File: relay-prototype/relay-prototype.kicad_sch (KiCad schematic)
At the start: 13 parts, among them K1 G5V-1

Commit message: schematic for adder, subtractor
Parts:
- removed K1, K? (x4): G5V-1, Relay_THT:Relay_SPDT_Omron_G5V-1, symbol Relay:G5V-1
- A0, A1, B0, B1: footprint (none) -> Button_Switch_THT:SW_DIP_SPSTx01_Slide_9.78x4.72mm_W7.62mm_P2.54mm
- R1, R2, R3, R4: footprint (none) -> Resistor_THT:R_Axial_DIN0207_L6.3mm_D2.5mm_P10.16mm_Horizontal
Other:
- added sheet page1 (page1.kicad_sch)

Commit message: prototype schematic finished for now
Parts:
- added D1 (x5): D_TVS, Diode_THT:D_DO-15_P12.70mm_Horizontal, symbol Device:D_TVS
- added K1 (x5): G5V-1, Relay_THT:Relay_SPDT_Omron_G5V-1, symbol Relay:G5V-1
- added LED1, LED2, LED3, LED4: LED, symbol Device:LED
- added R5, R6, R7, R8: 300, Resistor_THT:R_Axial_DIN0207_L6.3mm_D2.5mm_P10.16mm_Horizontal, symbol Device:R
- added R9: 100k, Resistor_THT:R_Axial_DIN0207_L6.3mm_D2.5mm_P10.16mm_Horizontal, symbol Device:R
- added S1: SW_DIP_x01, Button_Switch_THT:SW_DIP_SPSTx01_Slide_9.78x4.72mm_W7.62mm_P2.54mm, symbol Switch:SW_DIP_x01
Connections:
- net +5V: now also K1.10, K1.10, K1.10, K1.10, K1.10, S1.1
- net A0: now also K1.5, K1.6; no longer A0.2, R1.2
- net A1: now also K1.5, K1.6; no longer A1.2, R2.2
- net B0: now also K1.5, K1.6; no longer B0.2, R3.2
- net B1: now also K1.5, K1.6; no longer B1.2, R4.2
- net GND: now also D1.1 (A1), D1.1 (A1), D1.1 (A1), D1.1 (A1), D1.1 (A1), K1.1, K1.1, K1.1, K1.1, K1.1, K1.2, K1.2, K1.2, K1.2, K1.2, LED1.1 (K), LED2.1 (K), LED3.1 (K), LED4.1 (K), R9.2
- new net: D1.2 (A2), K1.9, R9.1, S1.2
- new net: A1.2, D1.2 (A2), K1.9, R2.2, R6.1
- new net: B1.2, D1.2 (A2), K1.9, R4.2, R8.1
- new net: A0.2, D1.2 (A2), K1.9, R1.2, R5.1
- new net: LED1.2 (A), R5.2
- new net: LED4.2 (A), R8.2
- new net: LED3.2 (A), R7.2
- new net: B0.2, D1.2 (A2), K1.9, R3.2, R7.1
- new net: LED2.2 (A), R6.2
- new net SELECT: K1.5, K1.6
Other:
- sheet page1 renamed ADD AND SUB
- added sheet MUX (page2.kicad_sch)
- moved on the sheet: A1, B0, B1, R2, R3, R4

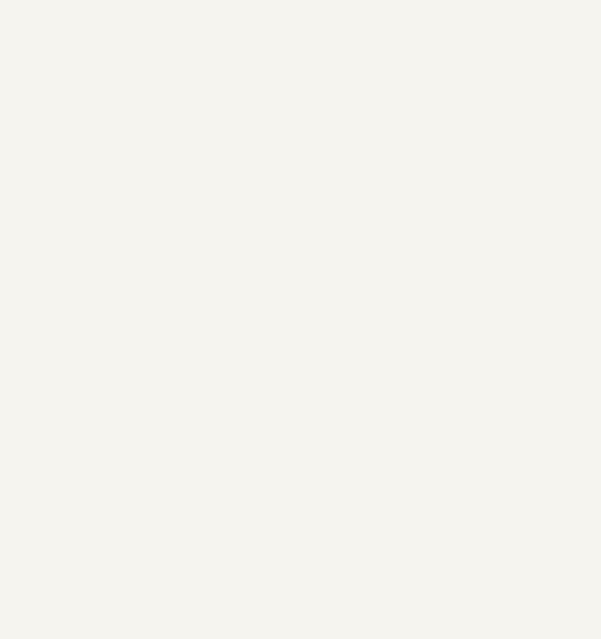
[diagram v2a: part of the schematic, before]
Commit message: start of pcb, usb-c connector
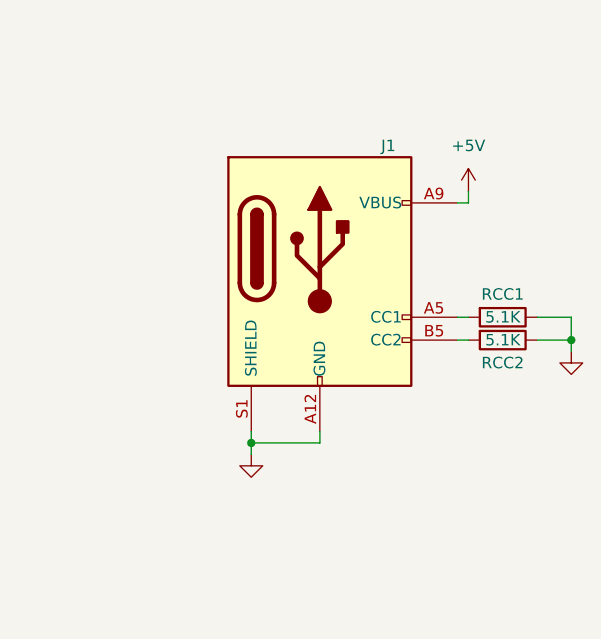
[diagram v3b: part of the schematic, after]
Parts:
- added J1: USB_C_Receptacle_PowerOnly_6P, USB-C-Power-tester:TYPE-C-31-M-17_handsolder, symbol Connector:USB_C_Receptacle_PowerOnly_6P
- added RCC1, RCC2: 5.1K, Resistor_THT:R_Axial_DIN0207_L6.3mm_D2.5mm_P10.16mm_Horizontal, symbol Device:R
- LED1, LED2, LED3, LED4: footprint (none) -> LED_THT:LED_D5.0mm
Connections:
- net +5V: now also J1.A9 (VBUS), J1.B9 (VBUS)
- net GND: now also J1.A12 (GND), J1.B12 (GND), J1.S1 (SHIELD), RCC1.1, RCC2.1
- new net: J1.A5 (CC1), RCC1.2
- new net: J1.B5 (CC2), RCC2.2
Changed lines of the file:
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@@
   (junction (at 27.94 91.44) (diameter 0) (color 0 0 0 0)
   )
+  (junction (at 199.39 45.72) (diameter 0) (color 0 0 0 0)
+  )
   (junction (at 95.25 86.36) (diameter 0) (color 0 0 0 0)
   )
@@
   (junction (at 87.63 91.44) (diameter 0) (color 0 0 0 0)
   )
+  (junction (at 163.83 57.15) (diameter 0) (color 0 0 0 0)
+  )
   (junction (at 95.25 62.23) (diameter 0) (color 0 0 0 0)
   )
@@
     (stroke (width 0) (type default))
   )
+  (wire (pts (xy 186.69 45.72) (xy 187.96 45.72))
+    (stroke (width 0) (type default))
+  )
   (wire (pts (xy 50.8 30.48) (xy 49.53 30.48))
     (stroke (width 0) (type default))
@@
     (stroke (width 0) (type default))
   )
+  (wire (pts (xy 163.83 55.88) (xy 163.83 57.15))
+    (stroke (width 0) (type default))
+  )
   (wire (pts (xy 58.42 97.79) (xy 59.69 97.79))
     (stroke (width 0) (type default))
@@
     (stroke (width 0) (type default))
   )
+  (wire (pts (xy 199.39 45.72) (xy 199.39 46.99))
+    (stroke (width 0) (type default))
+  )
   (wire (pts (xy 27.94 69.85) (xy 30.48 69.85))
     (stroke (width 0) (type default))
@@
     (stroke (width 0) (type default))
   )
+  (wire (pts (xy 171.45 57.15) (xy 171.45 55.88))
+    (stroke (width 0) (type default))
+  )
   (wire (pts (xy 78.74 52.07) (xy 80.01 52.07))
     (stroke (width 0) (type default))
@@
     (stroke (width 0) (type default))
   )
+  (wire (pts (xy 163.83 57.15) (xy 171.45 57.15))
+    (stroke (width 0) (type default))
+  )
   (wire (pts (xy 87.63 24.13) (xy 95.25 24.13))
     (stroke (width 0) (type default))
@@
     (stroke (width 0) (type default))
   )
+  (wire (pts (xy 195.58 43.18) (xy 199.39 43.18))
+    (stroke (width 0) (type default))
+  )
   (wire (pts (xy 80.01 91.44) (xy 87.63 91.44))
     (stroke (width 0) (type default))
@@
     (stroke (width 0) (type default))
   )
+  (wire (pts (xy 163.83 58.42) (xy 163.83 57.15))
+    (stroke (width 0) (type default))
+  )
   (wire (pts (xy 111.76 91.44) (xy 105.41 91.44))
     (stroke (width 0) (type default))
@@
     (stroke (width 0) (type default))
   )
+  (wire (pts (xy 187.96 29.21) (xy 187.96 30.48))
+    (stroke (width 0) (type default))
+  )
   (wire (pts (xy 87.63 123.19) (xy 87.63 128.27))
     (stroke (width 0) (type default))
@@
     (stroke (width 0) (type default))
   )
+  (wire (pts (xy 199.39 43.18) (xy 199.39 45.72))
+    (stroke (width 0) (type default))
+  )
   (wire (pts (xy 59.69 125.73) (xy 59.69 123.19))
     (stroke (width 0) (type default))
@@
     (stroke (width 0) (type default))
   )
+  (wire (pts (xy 187.96 30.48) (xy 186.69 30.48))
+    (stroke (width 0) (type default))
+  )
   (wire (pts (xy 105.41 24.13) (xy 105.41 25.4))
     (stroke (width 0) (type default))
@@
     (stroke (width 0) (type default))
   )
+  (wire (pts (xy 195.58 45.72) (xy 199.39 45.72))
+    (stroke (width 0) (type default))
+  )
   (wire (pts (xy 111.76 69.85) (xy 105.41 69.85))
     (stroke (width 0) (type default))
@@
   )
   (wire (pts (xy 95.25 69.85) (xy 95.25 71.12))
+    (stroke (width 0) (type default))
+  )
+  (wire (pts (xy 186.69 43.18) (xy 187.96 43.18))
     (stroke (width 0) (type default))
   )
@@
     )
   )
+  (symbol (lib_id "Device:R") (at 191.77 43.18 270) (unit 1)
+    (in_bom yes) (on_board yes) (dnp no)
+    (property "Reference" "RCC1" (at 191.77 40.64 90)
+      (effects (font (size 1.27 1.27)))
+    )
+    (property "Value" "5.1K" (at 191.77 43.18 90)
+      (effects (font (size 1.27 1.27)))
+    )
+    (property "Footprint" "Resistor_THT:R_Axial_DIN0207_L6.3mm_D2.5mm_P10.16mm_Horizontal" (at 191.77 41.402 90)
+      (effects (font (size 1.27 1.27)) hide)
+    )
+    (property "Datasheet" "~" (at 191.77 43.18 0)
+      (effects (font (size 1.27 1.27)) hide)
+    )
+    (pin "1")
+    (pin "2")
+    (instances
+      (project "relay-prototype"
+        (path "/732a1c84-589d-4882-93e4-2a6e3ba68e4c"
+          (reference "RCC1") (unit 1)
+        )
+      )
+    )
+  )
   (symbol (lib_id "Device:LED") (at 66.04 97.79 0) (unit 1)
     (in_bom yes) (on_board yes) (dnp no)
@@
       (effects (font (size 1.27 1.27)) hide)
     )
-    (property "Footprint" "" (at 66.04 97.79 0)
+    (property "Footprint" "LED_THT:LED_D5.0mm" (at 66.04 97.79 0)
       (effects (font (size 1.27 1.27)) hide)
     )
@@
     )
   )
+  (symbol (lib_id "Connector:USB_C_Receptacle_PowerOnly_6P") (at 171.45 38.1 0) (unit 1)
+    (in_bom yes) (on_board yes) (dnp no)
+    (property "Reference" "J1" (at 179.07 24.13 0)
+      (effects (font (size 1.27 1.27)))
+    )
+    (property "Value" "USB_C_Receptacle_PowerOnly_6P" (at 171.45 24.13 0)
+      (effects (font (size 1.27 1.27)) hide)
+    )
+    (property "Footprint" "USB-C-Power-tester:TYPE-C-31-M-17_handsolder" (at 175.26 35.56 0)
+      (effects (font (size 1.27 1.27)) hide)
+    )
+    (property "Datasheet" "https://www.usb.org/sites/default/files/documents/usb_type-c.zip" (at 171.45 38.1 0)
+      (effects (font (size 1.27 1.27)) hide)
+    )
+    (pin "A12")
+    (pin "A5")
+    (pin "A9")
+    (pin "B12")
+    (pin "B5")
+    (pin "B9")
+    (pin "S1")
+    (instances
+      (project "relay-prototype"
+        (path "/732a1c84-589d-4882-93e4-2a6e3ba68e4c"
+          (reference "J1") (unit 1)
+        )
+      )
+    )
+  )
   (symbol (lib_id "Device:R") (at 74.93 97.79 270) (unit 1)
     (in_bom yes) (on_board yes) (dnp no)
@@
       (effects (font (size 1.27 1.27)) hide)
     )
-    (property "Footprint" "" (at 66.04 76.2 0)
+    (property "Footprint" "LED_THT:LED_D5.0mm" (at 66.04 76.2 0)
       (effects (font (size 1.27 1.27)) hide)
     )
@@
       (effects (font (size 1.27 1.27)) hide)
     )
-    (property "Footprint" "" (at 66.04 30.48 0)
+    (property "Footprint" "LED_THT:LED_D5.0mm" (at 66.04 30.48 0)
       (effects (font (size 1.27 1.27)) hide)
     )
@@
         (path "/732a1c84-589d-4882-93e4-2a6e3ba68e4c"
           (reference "R6") (unit 1)
+        )
+      )
+    )
+  )
+  (symbol (lib_id "Device:R") (at 191.77 45.72 270) (unit 1)
+    (in_bom yes) (on_board yes) (dnp no)
+    (property "Reference" "RCC2" (at 191.77 48.26 90)
+      (effects (font (size 1.27 1.27)))
+    )
+    (property "Value" "5.1K" (at 191.77 45.72 90)
+      (effects (font (size 1.27 1.27)))
+    )
+    (property "Footprint" "Resistor_THT:R_Axial_DIN0207_L6.3mm_D2.5mm_P10.16mm_Horizontal" (at 191.77 43.942 90)
+      (effects (font (size 1.27 1.27)) hide)
+    )
+    (property "Datasheet" "~" (at 191.77 45.72 0)
+      (effects (font (size 1.27 1.27)) hide)
+    )
+    (pin "1")
+    (pin "2")
+    (instances
+      (project "relay-prototype"
+        (path "/732a1c84-589d-4882-93e4-2a6e3ba68e4c"
+          (reference "RCC2") (unit 1)
         )
       )
@@
         (path "/732a1c84-589d-4882-93e4-2a6e3ba68e4c"
           (reference "#PWR012") (unit 1)
+        )
+      )
+    )
+  )
+  (symbol (lib_id "power:GND") (at 199.39 46.99 0) (unit 1)
+    (in_bom yes) (on_board yes) (dnp no)
+    (property "Reference" "#PWR0118" (at 199.39 53.34 0)
+      (effects (font (size 1.27 1.27)) hide)
+    )
+    (property "Value" "GND" (at 199.39 50.8 0)
+      (effects (font (size 1.27 1.27)) hide)
+    )
+    (property "Footprint" "" (at 199.39 46.99 0)
+      (effects (font (size 1.27 1.27)) hide)
+    )
+    (property "Datasheet" "" (at 199.39 46.99 0)
+      (effects (font (size 1.27 1.27)) hide)
+    )
+    (pin "1")
+    (instances
+      (project "relay-prototype"
+        (path "/732a1c84-589d-4882-93e4-2a6e3ba68e4c/78cd5e50-4bfe-46a0-b184-d856f8a3b285"
+          (reference "#PWR0118") (unit 1)
+        )
+        (path "/732a1c84-589d-4882-93e4-2a6e3ba68e4c"
+          (reference "#PWR027") (unit 1)
         )
       )
@@
     )
   )
+  (symbol (lib_id "power:GND") (at 163.83 58.42 0) (unit 1)
+    (in_bom yes) (on_board yes) (dnp no)
+    (property "Reference" "#PWR0118" (at 163.83 64.77 0)
+      (effects (font (size 1.27 1.27)) hide)
+    )
+    (property "Value" "GND" (at 163.83 62.23 0)
+      (effects (font (size 1.27 1.27)) hide)
+    )
+    (property "Footprint" "" (at 163.83 58.42 0)
+      (effects (font (size 1.27 1.27)) hide)
+    )
+    (property "Datasheet" "" (at 163.83 58.42 0)
+      (effects (font (size 1.27 1.27)) hide)
+    )
+    (pin "1")
+    (instances
+      (project "relay-prototype"
+        (path "/732a1c84-589d-4882-93e4-2a6e3ba68e4c/78cd5e50-4bfe-46a0-b184-d856f8a3b285"
+          (reference "#PWR0118") (unit 1)
+        )
+        (path "/732a1c84-589d-4882-93e4-2a6e3ba68e4c"
+          (reference "#PWR026") (unit 1)
+        )
+      )
+    )
+  )
   (symbol (lib_id "power:GND") (at 102.87 62.23 0) (unit 1)
     (in_bom yes) (on_board yes) (dnp no)
@@
       (effects (font (size 1.27 1.27)) hide)
     )
-    (property "Footprint" "" (at 66.04 52.07 0)
+    (property "Footprint" "LED_THT:LED_D5.0mm" (at 66.04 52.07 0)
       (effects (font (size 1.27 1.27)) hide)
     )
@@
         )
       )
+    )
+  )
+  (symbol (lib_id "power:+5V") (at 187.96 29.21 0) (unit 1)
+    (in_bom yes) (on_board yes) (dnp no) (fields_autoplaced)
+    (property "Reference" "#PWR025" (at 187.96 33.02 0)
+      (effects (font (size 1.27 1.27)) hide)
+    )
+    (property "Value" "+5V" (at 187.96 24.13 0)
+      (effects (font (size 1.27 1.27)))
+    )
+    (property "Footprint" "" (at 187.96 29.21 0)
+      (effects (font (size 1.27 1.27)) hide)
+    )
+    (property "Datasheet" "" (at 187.96 29.21 0)
+      (effects (font (size 1.27 1.27)) hide)
+    )
+    (pin "1")
+    (instances
+      (project "relay-prototype"
+        (path "/732a1c84-589d-4882-93e4-2a6e3ba68e4c"
+          (reference "#PWR025") (unit 1)
+        )
+      )

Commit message: prototype board completed, usb 3d model added
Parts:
- A0: Part_Link (none) -> https://www.digikey.com/short/8h484j23
- D1: footprint Diode_THT:D_DO-15_P12.70mm_Horizontal -> Diode_SMD:D_SOD-323_HandSoldering
- J1: Part_Link (none) -> https://www.digikey.com/short/1h24z481
- LED1: Part_Link (none) -> https://www.digikey.com/short/hfd7qn10
- R1: Part_Link (none) -> https://www.digikey.com/short/9cb8r38z
- R5: value 300 -> 330; Part_Link (none) -> https://www.digikey.com/short/ntdtzv7z
- R6, R7, R8: value 300 -> 330
- RCC1: Part_Link (none) -> https://www.digikey.com/short/5zr5m407
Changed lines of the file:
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@@
       (effects (font (size 1.27 1.27)) (justify right) hide)
     )
-    (property "Footprint" "Diode_THT:D_DO-15_P12.70mm_Horizontal" (at 87.63 132.08 0)
+    (property "Footprint" "Diode_SMD:D_SOD-323_HandSoldering" (at 87.63 132.08 0)
       (effects (font (size 1.27 1.27)) hide)
     )
@@
       (effects (font (size 1.27 1.27)))
     )
-    (property "Value" "300" (at 74.93 30.48 90)
+    (property "Value" "330" (at 74.93 30.48 90)
       (effects (font (size 1.27 1.27)))
     )
@@
       (effects (font (size 1.27 1.27)) hide)
     )
+    (property "Part_Link" "https://www.digikey.com/short/ntdtzv7z" (at 74.93 30.48 90)
+      (effects (font (size 1.27 1.27)) hide)
+    )
     (pin "1")
     (pin "2")
@@
     )
     (property "Datasheet" "~" (at 191.77 43.18 0)
+      (effects (font (size 1.27 1.27)) hide)
+    )
+    (property "Part_Link" "https://www.digikey.com/short/5zr5m407" (at 191.77 43.18 90)
       (effects (font (size 1.27 1.27)) hide)
     )
@@
     )
     (property "Datasheet" "https://www.usb.org/sites/default/files/documents/usb_type-c.zip" (at 171.45 38.1 0)
+      (effects (font (size 1.27 1.27)) hide)
+    )
+    (property "Part_Link" "https://www.digikey.com/short/1h24z481" (at 171.45 38.1 0)
       (effects (font (size 1.27 1.27)) hide)
     )
@@
       (effects (font (size 1.27 1.27)))
     )
-    (property "Value" "300" (at 74.93 97.79 90)
+    (property "Value" "330" (at 74.93 97.79 90)
       (effects (font (size 1.27 1.27)))
     )
@@
       (effects (font (size 1.27 1.27)) (justify right) hide)
     )
-    (property "Footprint" "Diode_THT:D_DO-15_P12.70mm_Horizontal" (at 87.63 33.02 0)
+    (property "Footprint" "Diode_SMD:D_SOD-323_HandSoldering" (at 87.63 33.02 0)
       (effects (font (size 1.27 1.27)) hide)
     )
@@
       (effects (font (size 1.27 1.27)) (justify right) hide)
     )
-    (property "Footprint" "Diode_THT:D_DO-15_P12.70mm_Horizontal" (at 87.63 100.33 0)
+    (property "Footprint" "Diode_SMD:D_SOD-323_HandSoldering" (at 87.63 100.33 0)
       (effects (font (size 1.27 1.27)) hide)
     )
@@
       (effects (font (size 1.27 1.27)) hide)
     )
+    (property "Part_Link" "https://www.digikey.com/short/hfd7qn10" (at 66.04 30.48 0)
+      (effects (font (size 1.27 1.27)) hide)
+    )
     (pin "1")
     (pin "2")
@@
       (effects (font (size 1.27 1.27)))
     )
-    (property "Value" "300" (at 74.93 76.2 90)
+    (property "Value" "330" (at 74.93 76.2 90)
       (effects (font (size 1.27 1.27)))
     )
@@
       (effects (font (size 1.27 1.27)))
     )
-    (property "Value" "300" (at 74.93 52.07 90)
+    (property "Value" "330" (at 74.93 52.07 90)
       (effects (font (size 1.27 1.27)))
     )
@@
     )
     (property "Datasheet" "~" (at 54.61 30.48 0)
+      (effects (font (size 1.27 1.27)) hide)
+    )
+    (property "Part_Link" "https://www.digikey.com/short/9cb8r38z" (at 54.61 30.48 90)
       (effects (font (size 1.27 1.27)) hide)
     )
@@
       (effects (font (size 1.27 1.27)) (justify right) hide)
     )
-    (property "Footprint" "Diode_THT:D_DO-15_P12.70mm_Horizontal" (at 87.63 54.61 0)
+    (property "Footprint" "Diode_SMD:D_SOD-323_HandSoldering" (at 87.63 54.61 0)
       (effects (font (size 1.27 1.27)) hide)
     )
@@
       (effects (font (size 1.27 1.27)) hide)
     )
+    (property "Part_Link" "https://www.digikey.com/short/8h484j23" (at 38.1 24.13 0)
+      (effects (font (size 1.27 1.27)) hide)
+    )
     (pin "1")
     (pin "2")
@@
       (effects (font (size 1.27 1.27)) (justify right) hide)
     )
-    (property "Footprint" "Diode_THT:D_DO-15_P12.70mm_Horizontal" (at 87.63 78.74 0)
-      (effects (font (size 1.27 1.27)) hide)
-    )
+    (property "Footprint" "Diode_SMD:D_SOD-323_HandSoldering" (at 87.63 78.74 0)
+      (effects (font (size 1.27 1.27)) hide)
+    )
